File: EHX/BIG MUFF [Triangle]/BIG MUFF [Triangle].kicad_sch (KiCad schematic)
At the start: 55 parts, among them J1 INPUT, J2 Power, J3 LED, J4 OUTPUT, Q1 2N3904, Q2 2N3904, Q3 2N3904, Q4 2N3904

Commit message: refactor: 見直しに伴う形式的な更新
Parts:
- renumbered J4 to J2, J2 to J3, J3 to J4
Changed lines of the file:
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@@
 		(dnp no)
 		(fields_autoplaced yes)
-		(property "Reference" "#PWR025"
+		(property "Reference" "#PWR024"
 			(at 260.35 139.7 0)
 			(hide yes)
@@
 			(project "BIG MUFF [Triangle]"
 				(path "/1184b22c-7f25-432e-b63b-19d9e238a94b"
-					(reference "#PWR025")
+					(reference "#PWR024")
 					(unit 1)
 				)
@@
 		(dnp no)
 		(fields_autoplaced yes)
-		(property "Reference" "J2"
+		(property "Reference" "J3"
 			(at 44.45 165.0999 0)
 			(show_name no)
@@
 			(project "BIG MUFF [Triangle]"
 				(path "/1184b22c-7f25-432e-b63b-19d9e238a94b"
-					(reference "J2")
+					(reference "J3")
 					(unit 1)
 				)
@@
 		(dnp no)
 		(fields_autoplaced yes)
-		(property "Reference" "J3"
+		(property "Reference" "J4"
 			(at 44.45 172.7199 0)
 			(show_name no)
@@
 			(project "BIG MUFF [Triangle]"
 				(path "/1184b22c-7f25-432e-b63b-19d9e238a94b"
-					(reference "J3")
+					(reference "J4")
 					(unit 1)
 				)
@@
 		(dnp no)
 		(fields_autoplaced yes)
-		(property "Reference" "#PWR020"
+		(property "Reference" "#PWR019"
 			(at 203.2 139.7 0)
 			(hide yes)
@@
 			(project "BIG MUFF [Triangle]"
 				(path "/1184b22c-7f25-432e-b63b-19d9e238a94b"
-					(reference "#PWR020")
+					(reference "#PWR019")
 					(unit 1)
 				)
@@
 		(dnp no)
 		(fields_autoplaced yes)
-		(property "Reference" "#PWR08"
+		(property "Reference" "#PWR07"
 			(at 69.85 139.7 0)
 			(hide yes)
@@
 			(project "BIG MUFF [Triangle]"
 				(path "/1184b22c-7f25-432e-b63b-19d9e238a94b"
-					(reference "#PWR08")
+					(reference "#PWR07")
 					(unit 1)
 				)
@@
 		(dnp no)
 		(fields_autoplaced yes)
-		(property "Reference" "J4"
+		(property "Reference" "J2"
 			(at 42.545 154.94 0)
 			(show_name no)
@@
 			(project "BIG MUFF [Triangle]"
 				(path "/1184b22c-7f25-432e-b63b-19d9e238a94b"
-					(reference "J4")
+					(reference "J2")
 					(unit 1)
 				)
@@
 		(dnp no)
 		(fields_autoplaced yes)
-		(property "Reference" "#PWR021"
+		(property "Reference" "#PWR020"
 			(at 222.25 67.31 0)
 			(hide yes)
@@
 			(project "BIG MUFF [Triangle]"
 				(path "/1184b22c-7f25-432e-b63b-19d9e238a94b"
-					(reference "#PWR021")
+					(reference "#PWR020")
 					(unit 1)
 				)
@@
 		(dnp no)
 		(fields_autoplaced yes)
-		(property "Reference" "#PWR05"
+		(property "Reference" "#PWR01"
 			(at 38.1 139.7 0)
 			(hide yes)
@@
 			(project "BIG MUFF [Triangle]"
 				(path "/1184b22c-7f25-432e-b63b-19d9e238a94b"
-					(reference "#PWR05")
+					(reference "#PWR01")
 					(unit 1)
 				)
@@
 		(dnp no)
 		(fields_autoplaced yes)
-		(property "Reference" "#PWR09"
+		(property "Reference" "#PWR08"
 			(at 76.2 177.8 0)
 			(hide yes)
@@
 			(project "BIG MUFF [Triangle]"
 				(path "/1184b22c-7f25-432e-b63b-19d9e238a94b"
-					(reference "#PWR09")
+					(reference "#PWR08")
 					(unit 1)
 				)
@@
 		(dnp no)
 		(fields_autoplaced yes)
-		(property "Reference" "#PWR019"
+		(property "Reference" "#PWR018"
 			(at 203.2 76.2 0)
 			(hide yes)
@@
 			(project "BIG MUFF [Triangle]"
 				(path "/1184b22c-7f25-432e-b63b-19d9e238a94b"
-					(reference "#PWR019")
+					(reference "#PWR018")
 					(unit 1)
 				)
@@
 		(dnp no)
 		(fields_autoplaced yes)
-		(property "Reference" "#PWR024"
+		(property "Reference" "#PWR023"
 			(at 234.95 139.7 0)
 			(hide yes)
@@
 			(project "BIG MUFF [Triangle]"
 				(path "/1184b22c-7f25-432e-b63b-19d9e238a94b"
-					(reference "#PWR024")
+					(reference "#PWR023")
 					(unit 1)
 				)
@@
 		(dnp no)
 		(fields_autoplaced yes)
-		(property "Reference" "#PWR011"
+		(property "Reference" "#PWR010"
 			(at 82.55 139.7 0)
 			(hide yes)
@@
 			(project "BIG MUFF [Triangle]"
 				(path "/1184b22c-7f25-432e-b63b-19d9e238a94b"
-					(reference "#PWR011")
+					(reference "#PWR010")
 					(unit 1)
 				)
@@
 		(dnp no)
 		(fields_autoplaced yes)
-		(property "Reference" "#PWR016"
+		(property "Reference" "#PWR015"
 			(at 165.1 139.7 0)
 			(hide yes)
@@
 			(project "BIG MUFF [Triangle]"
 				(path "/1184b22c-7f25-432e-b63b-19d9e238a94b"
-					(reference "#PWR016")
+					(reference "#PWR015")
 					(unit 1)
 				)
@@
 		(dnp no)
 		(fields_autoplaced yes)
-		(property "Reference" "#PWR015"
+		(property "Reference" "#PWR014"
 			(at 139.7 139.7 0)
 			(hide yes)
@@
 			(project "BIG MUFF [Triangle]"
 				(path "/1184b22c-7f25-432e-b63b-19d9e238a94b"
-					(reference "#PWR015")
+					(reference "#PWR014")
 					(unit 1)
 				)
@@
 		(dnp no)
 		(fields_autoplaced yes)
-		(property "Reference" "#PWR013"
+		(property "Reference" "#PWR012"
 			(at 127 139.7 0)
 			(hide yes)
@@
 			(project "BIG MUFF [Triangle]"
 				(path "/1184b22c-7f25-432e-b63b-19d9e238a94b"
-					(reference "#PWR013")
+					(reference "#PWR012")
 					(unit 1)
 				)
@@
 		(dnp no)
 		(fields_autoplaced yes)
-		(property "Reference" "#PWR012"
+		(property "Reference" "#PWR011"
 			(at 95.25 139.7 0)
 			(hide yes)
@@
 			(project "BIG MUFF [Triangle]"
 				(path "/1184b22c-7f25-432e-b63b-19d9e238a94b"
-					(reference "#PWR012")
+					(reference "#PWR011")
 					(unit 1)
 				)
@@
 		(dnp no)
 		(fields_autoplaced yes)
-		(property "Reference" "#PWR017"
+		(property "Reference" "#PWR016"
 			(at 177.8 67.31 0)
 			(hide yes)
@@
 			(project "BIG MUFF [Triangle]"
 				(path "/1184b22c-7f25-432e-b63b-19d9e238a94b"
-					(reference "#PWR017")
+					(reference "#PWR016")
 					(unit 1)
 				)
@@
 		(dnp no)
 		(fields_autoplaced yes)
-		(property "Reference" "#PWR023"
+		(property "Reference" "#PWR022"
 			(at 234.95 67.31 0)
 			(hide yes)
@@
 			(project "BIG MUFF [Triangle]"
 				(path "/1184b22c-7f25-432e-b63b-19d9e238a94b"
-					(reference "#PWR023")
+					(reference "#PWR022")
 					(unit 1)
 				)
@@
 		(dnp no)
 		(fields_autoplaced yes)
-		(property "Reference" "#PWR06"
+		(property "Reference" "#PWR05"
 			(at 63.5 162.56 0)
 			(hide yes)
@@
 			(project "BIG MUFF [Triangle]"
 				(path "/1184b22c-7f25-432e-b63b-19d9e238a94b"
-					(reference "#PWR06")
+					(reference "#PWR05")
 					(unit 1)
 				)
@@
 		(dnp no)
 		(fields_autoplaced yes)
-		(property "Reference" "#PWR022"
+		(property "Reference" "#PWR021"
 			(at 222.25 139.7 0)
 			(hide yes)
@@
 			(project "BIG MUFF [Triangle]"
 				(path "/1184b22c-7f25-432e-b63b-19d9e238a94b"
-					(reference "#PWR022")
+					(reference "#PWR021")
 					(unit 1)
 				)
@@
 		(dnp no)
 		(fields_autoplaced yes)
-		(property "Reference" "#PWR07"
+		(property "Reference" "#PWR06"
 			(at 63.5 177.8 0)
 			(hide yes)
@@
 			(project "BIG MUFF [Triangle]"
 				(path "/1184b22c-7f25-432e-b63b-19d9e238a94b"
-					(reference "#PWR07")
+					(reference "#PWR06")
 					(unit 1)
 				)
@@
 		(dnp no)
 		(fields_autoplaced yes)
-		(property "Reference" "#PWR014"
+		(property "Reference" "#PWR013"
 			(at 139.7 67.31 0)
 			(hide yes)
@@
 			(project "BIG MUFF [Triangle]"
 				(path "/1184b22c-7f25-432e-b63b-19d9e238a94b"
-					(reference "#PWR014")
+					(reference "#PWR013")
 					(unit 1)
 				)
@@
 		(dnp no)
 		(fields_autoplaced yes)
-		(property "Reference" "#PWR018"
+		(property "Reference" "#PWR017"
 			(at 177.8 139.7 0)
 			(hide yes)
@@
 			(project "BIG MUFF [Triangle]"
 				(path "/1184b22c-7f25-432e-b63b-19d9e238a94b"
-					(reference "#PWR018")
+					(reference "#PWR017")
 					(unit 1)
 				)
@@
 		(dnp no)
 		(fields_autoplaced yes)
-		(property "Reference" "#PWR010"
+		(property "Reference" "#PWR09"
 			(at 82.55 67.31 0)
 			(hide yes)
@@
 			(project "BIG MUFF [Triangle]"
 				(path "/1184b22c-7f25-432e-b63b-19d9e238a94b"
-					(reference "#PWR010")
+					(reference "#PWR09")
 					(unit 1)
 				)

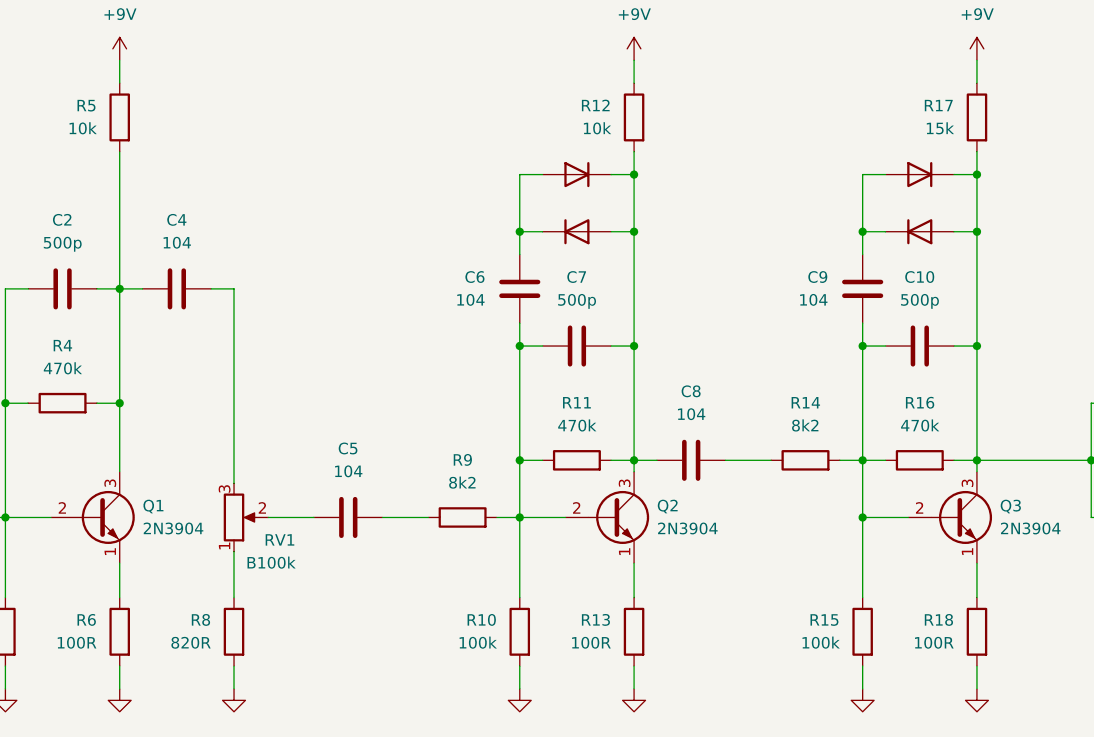
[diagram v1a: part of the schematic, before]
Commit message: fix: 1N4148のフットプリントが小さすぎた
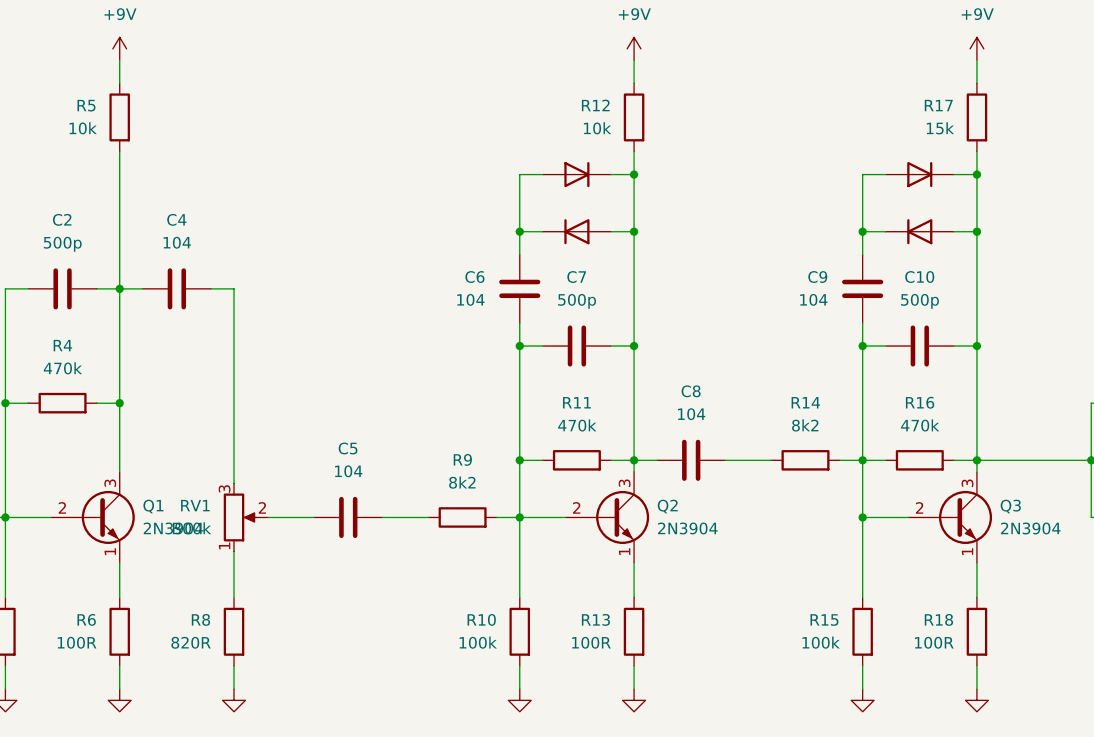
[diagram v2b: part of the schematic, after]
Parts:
- removed D3, D4, D5, D6: 1N4148, Diode_THT:D_DO-35_SOD27_P3.81mm_Vertical_AnodeUp, symbol Diode:1N4148
- added D10, D7, D8, D9: 1N4148, Diode_THT:D_DO-35_SOD27_P5.08mm_Vertical_AnodeUp, symbol Diode:1N4148
- RV1: value B100k -> B00k
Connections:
- net at C10.2, C11.1, Q3.3 (C)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: now also D10.1 (K), D9.2 (A)
- net at C9.1: now also D10.2 (A), D9.1 (K)
- net at C6.1: now also D7.1 (K), D8.2 (A)
- net at C7.2, C8.1, Q2.3 (C)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: now also D7.2 (A), D8.1 (K)
